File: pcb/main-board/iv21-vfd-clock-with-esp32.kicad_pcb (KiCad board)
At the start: 2 copper layers, 101.5 x 40 mm, 29 parts, among them J1 Conn_02x10_Odd_Even, J2 4328, P1 USB_C_Plug_USB2.0, SW1 SW_SPST, SW2 SW_SPST, U1 MAX6921AQI_, U2 MOUDLE-SEEEDUINO-XIAO-ESP32C3, U3 AP3012, U4 S-1167B24

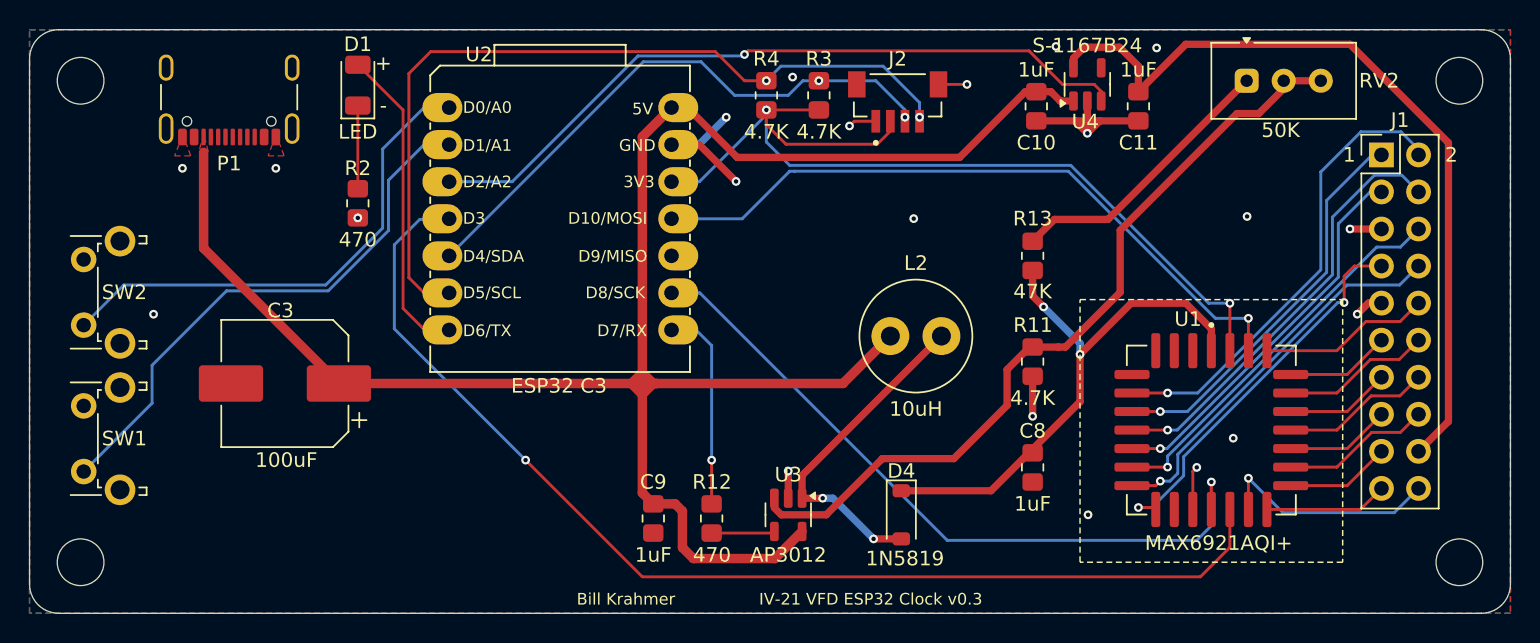
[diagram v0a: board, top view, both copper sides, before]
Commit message: Some trace updates.
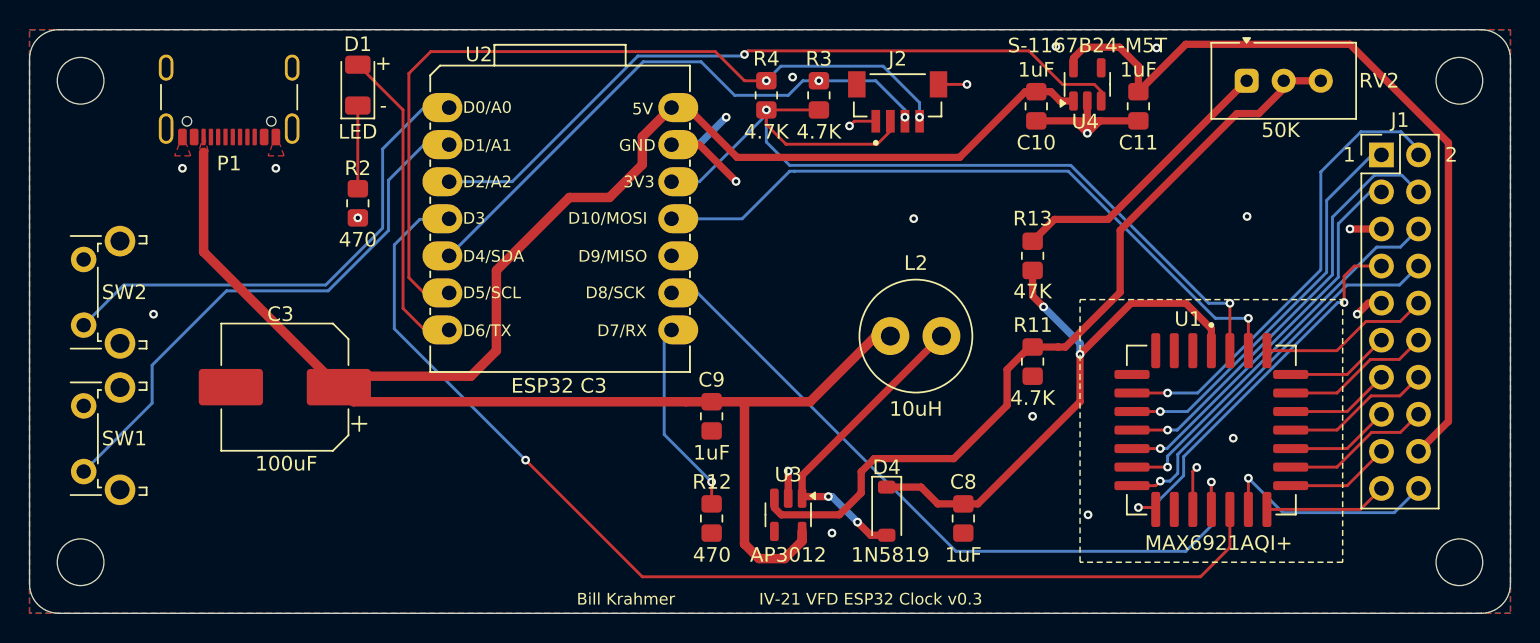
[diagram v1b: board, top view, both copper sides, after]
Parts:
- U4: value S-1167B24 -> S-1167B24-M5T
- moved C9 8.06 mm to (81.8, 44.5)
- moved C8 5.90 mm to (99.0, 51.5)
- moved D4 1.03 mm to (93.8, 51.0)
- moved C3 0.25 mm to (52.5, 42.5)
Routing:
- net /5V: track 137.1 -> 141.9 mm
- net Net-(U3-~{SHDN}): track 4.35 -> 0.16 mm
- net GND: track 37.2 -> 34.5 mm, vias 21 -> 22
- net /VPP: track 37.9 -> 39.6 mm
- net Net-(D4-A): track 23.0 -> 22.0 mm
- net Net-(U3-FB): track 54.9 -> 55.7 mm
- net Net-(U1-CLK): track 49.3 -> 49.9 mm
- net Net-(U2-PB09_A7_D7_RX): track 14.0 -> 13.5 mm

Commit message: change resistor value.
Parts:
- R13: value 47K -> 75K
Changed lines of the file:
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@@
 			)
 		)
-		(property "Value" "47K"
+		(property "Value" "75K"
 			(at -2.45 0 0)
 			(layer "F.SilkS")

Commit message: ...
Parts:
- moved C9 1.00 mm to (80.8, 44.5)
- moved R12 1.00 mm to (80.8, 51.5)
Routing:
- net Net-(U3-~{SHDN}): track 0.16 -> 5.51 mm, vias 0 -> 2
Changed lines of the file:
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@@
 	(footprint "Resistor_SMD:R_0805_2012Metric_Pad1.20x1.40mm_HandSolder"
 		(layer "F.Cu")
-		(at 81.75 51.5 -90)
+		(at 80.75 51.5 -90)
 		(descr "Resistor SMD 0805 (2012 Metric), square (rectangular) end terminal, IPC-7351 nominal with elongated pad for handsoldering. (Body size source: IPC-SM-782 page 72, https://www.pcb-3d.com/wordpress/wp-content/uploads/ipc-sm-782a_amendment_1_and_2.pdf), generated with kicad-footprint-generator")
 		(tags "resistor handsolder")
@@
 	(footprint "Resistor_SMD:R_0805_2012Metric_Pad1.20x1.40mm_HandSolder"
 		(layer "F.Cu")
-		(at 81.75 44.5 -90)
+		(at 80.75 44.5 -90)
 		(descr "Resistor SMD 0805 (2012 Metric), square (rectangular) end terminal, IPC-7351 nominal with elongated pad for handsoldering. (Body size source: IPC-SM-782 page 72, https://www.pcb-3d.com/wordpress/wp-content/uploads/ipc-sm-782a_amendment_1_and_2.pdf), generated with kicad-footprint-generator")
 		(tags "resistor handsolder")
@@
 	)
 	(segment
+		(start 80.75 43.5)
+		(end 57.2 43.5)
+		(width 0.65)
+		(layer "F.Cu")
+		(net 11)
+	)
+	(segment
 		(start 85 54.25)
 		(end 84 53.25)
@@
 	)
 	(segment
-		(start 57.2 43.5)
-		(end 56.2 42.5)
-		(width 0.65)
-		(layer "F.Cu")
-		(net 11)
-	)
-	(segment
 		(start 79 23.34)
 		(end 77 25.34)
@@
 	)
 	(segment
-		(start 81.75 43.5)
-		(end 80 43.5)
+		(start 57.2 43.5)
+		(end 56.2 42.5)
 		(width 0.65)
 		(layer "F.Cu")
@@
 	)
 	(segment
-		(start 80 43.5)
-		(end 57.2 43.5)
-		(width 0.65)
-		(layer "F.Cu")
-		(net 11)
-	)
-	(segment
 		(start 88.5 43.5)
 		(end 84 43.5)
@@
 	(segment
 		(start 84 43.5)
-		(end 81.75 43.5)
+		(end 80.75 43.5)
 		(width 0.65)
 		(layer "F.Cu")
@@
 		(net 39)
 	)
+	(via
+		(at 80.75 52.5)
+		(size 0.6)
+		(drill 0.3)
+		(layers "F.Cu" "B.Cu")
+		(net 39)
+	)
+	(via
+		(at 86.05 52.3875)
+		(size 0.6)
+		(drill 0.3)
+		(layers "F.Cu" "B.Cu")
+		(net 39)
+	)
 	(segment
-		(start 81.75 50.5)
-		(end 81.75 49)
+		(start 86.05 52.3875)
+		(end 80.8625 52.3875)
+		(width 0.2)
+		(layer "B.Cu")
+		(net 39)
+	)
+	(segment
+		(start 80.8625 52.3875)
+		(end 80.75 52.5)
+		(width 0.2)
+		(layer "B.Cu")
+		(net 39)
+	)
+	(segment
+		(start 80.75 49)
+		(end 80.75 50.5)
 		(width 0.2)
 		(layer "F.Cu")
@@
 	)
 	(via
-		(at 81.75 49)
+		(at 80.75 49)
 		(size 0.6)
 		(drill 0.3)
@@
 	)
 	(segment
-		(start 78.5 45.75)
+		(start 78.5 46.75)
 		(end 78.5 39.08)
 		(width 0.2)
@@
 	)
 	(segment
-		(start 78.5 39.08)
-		(end 79 38.58)
+		(start 80.75 49)
+		(end 78.5 46.75)
 		(width 0.2)
 		(layer "B.Cu")
@@
 	)
 	(segment
-		(start 81.75 49)
-		(end 78.5 45.75)
+		(start 78.5 39.08)
+		(end 79 38.58)
 		(width 0.2)
 		(layer "B.Cu")

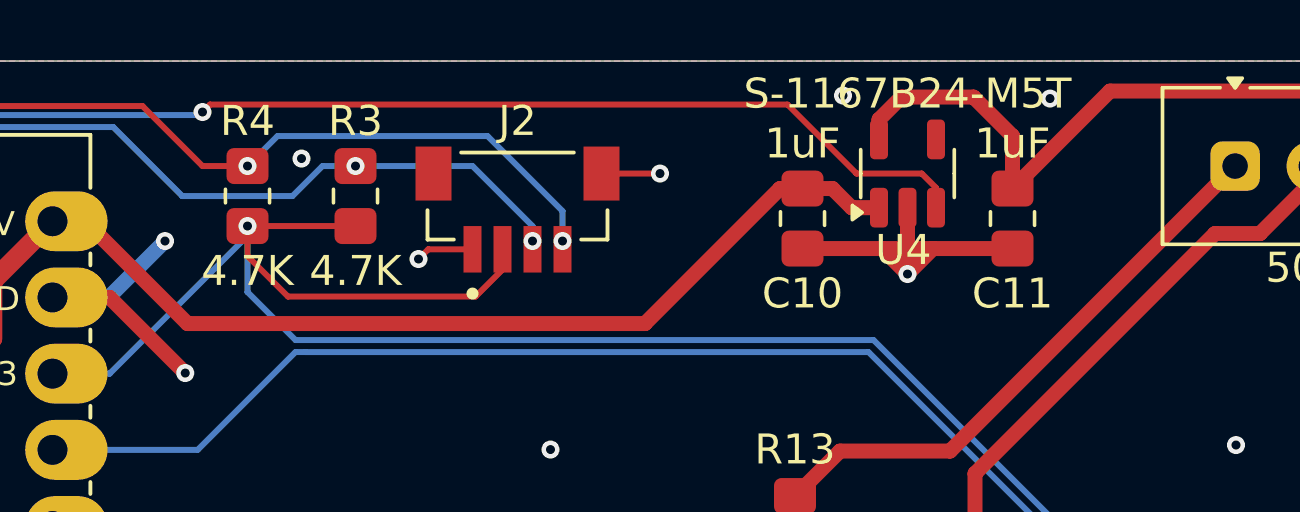
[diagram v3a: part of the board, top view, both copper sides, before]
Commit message: Add 470R resistor to S-1167B24 on/off pin
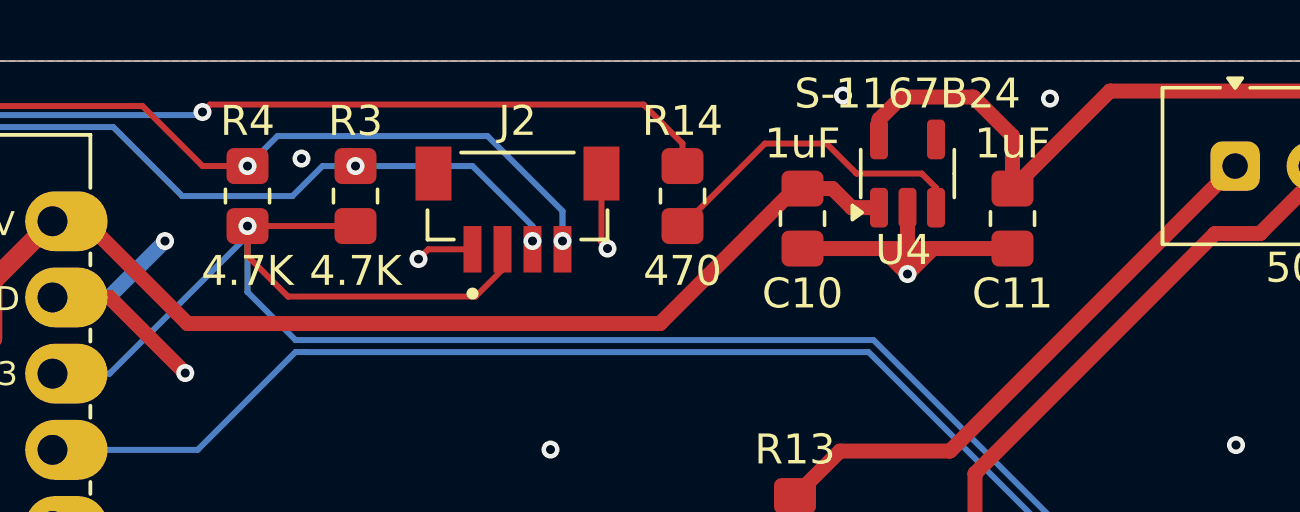
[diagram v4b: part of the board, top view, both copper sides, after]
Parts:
- added R14: 470, Resistor_SMD:R_0805_2012Metric_Pad1.20x1.40mm_HandSolder, F.Cu at (100.0, 22.5)
- U4: value S-1167B24-M5T -> S-1167B24
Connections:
- U4 pad 3: Net-(U2-PA10_A2_D2) -> Net-(U4-ON/~{OFF})
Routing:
- net Net-(U4-ON/~{OFF}): track 0.00 -> 10.9 mm
- net Net-(U2-PA10_A2_D2): track 50.2 -> 41.2 mm
- net GND: track 34.5 -> 35.1 mm
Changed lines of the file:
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@@
 	(net 52 "unconnected-(P1-SHIELD-PadS1)_2")
 	(net 53 "Net-(R13-Pad2)")
+	(net 54 "Net-(U4-ON{slash}~{OFF})")
 	(footprint "Diode_SMD:D_SOD-123"
 		(layer "F.Cu")
@@
 			)
 		)
-		(property "Value" "S-1167B24-M5T"
+		(property "Value" "S-1167B24"
 			(at 2.6625 0 0)
 			(layer "F.SilkS")
@@
 			(layers "F.Cu" "F.Mask" "F.Paste")
 			(roundrect_rratio 0.25)
-			(net 41 "Net-(U2-PA10_A2_D2)")
+			(net 54 "Net-(U4-ON{slash}~{OFF})")
 			(pinfunction "ON/~{OFF}")
 			(pintype "input")
@@
 		)
 	)
+	(footprint "Resistor_SMD:R_0805_2012Metric_Pad1.20x1.40mm_HandSolder"
+		(layer "F.Cu")
+		(at 100 22.5 90)
+		(descr "Resistor SMD 0805 (2012 Metric), square (rectangular) end terminal, IPC-7351 nominal with elongated pad for handsoldering. (Body size source: IPC-SM-782 page 72, https://www.pcb-3d.com/wordpress/wp-content/uploads/ipc-sm-782a_amendment_1_and_2.pdf), generated with kicad-footprint-generator")
+		(tags "resistor handsolder")
+		(property "Reference" "R14"
+			(at 2.5 0 0)
+			(layer "F.SilkS")
+			(effects
+				(font
+					(size 1 1)
+					(thickness 0.15)
+				)
+			)
+		)
+		(property "Value" "470"
+			(at -2.5 0 0)
+			(layer "F.SilkS")
+			(effects
+				(font
+					(size 1 1)
+					(thickness 0.15)
+				)
+			)
+		)
+		(property "Datasheet" ""
+			(at 0 0 90)
+			(layer "F.Fab")
+			(hide yes)
+			(effects
+				(font
+					(size 1.27 1.27)
+					(thickness 0.15)
+				)
+			)
+		)
+		(property "Description" "Resistor, US symbol"
+			(at 0 0 90)
+			(layer "F.Fab")
+			(hide yes)
+			(effects
+				(font
+					(size 1.27 1.27)
+					(thickness 0.15)
+				)
+			)
+		)
+		(property ki_fp_filters "R_*")
+		(sheetname "/")
+		(sheetfile "iv21-vfd-clock-with-esp32.kicad_sch")
+		(attr smd)
+		(fp_line
+			(start -0.227064 -0.735)
+			(end 0.227064 -0.735)
+			(stroke
+				(width 0.12)
+				(type solid)
+			)
+			(layer "F.SilkS")
+		)
+		(fp_line
+			(start -0.227064 0.735)
+			(end 0.227064 0.735)
+			(stroke
+				(width 0.12)
+				(type solid)
+			)
+			(layer "F.SilkS")
+		)
+		(fp_line
+			(start 1.85 -0.95)
+			(end 1.85 0.95)
+			(stroke
+				(width 0.05)
+				(type solid)
+			)
+			(layer "F.CrtYd")
+		)
+		(fp_line
+			(start -1.85 -0.95)
+			(end 1.85 -0.95)
+			(stroke
+				(width 0.05)
+				(type solid)
+			)
+			(layer "F.CrtYd")
+		)
+		(fp_line
+			(start 1.85 0.95)
+			(end -1.85 0.95)
+			(stroke
+				(width 0.05)
+				(type solid)
+			)
+			(layer "F.CrtYd")
+		)
+		(fp_line
+			(start -1.85 0.95)
+			(end -1.85 -0.95)
+			(stroke
+				(width 0.05)
+				(type solid)
+			)
+			(layer "F.CrtYd")
+		)
+		(fp_line
+			(start 1 -0.625)
+			(end 1 0.625)
+			(stroke
+				(width 0.1)
+				(type solid)
+			)
+			(layer "F.Fab")
+		)
+		(fp_line
+			(start -1 -0.625)
+			(end 1 -0.625)
+			(stroke
+				(width 0.1)
+				(type solid)
+			)
+			(layer "F.Fab")
+		)
+		(fp_line
+			(start 1 0.625)
+			(end -1 0.625)
+			(stroke
+				(width 0.1)
+				(type solid)
+			)
+			(layer "F.Fab")
+		)
+		(fp_line
+			(start -1 0.625)
+			(end -1 -0.625)
+			(stroke
+				(width 0.1)
+				(type solid)
+			)
+			(layer "F.Fab")
+		)
+		(fp_text user "${REFERENCE}"
+			(at 0 0 90)
+			(layer "F.Fab")
+			(effects
+				(font
+					(size 0.5 0.5)
+					(thickness 0.08)
+				)
+			)
+		)
+		(pad "1" smd roundrect
+			(at -1 0 90)
+			(size 1.2 1.4)
+			(layers "F.Cu" "F.Mask" "F.Paste")
+			(roundrect_rratio 0.208333)
+			(net 54 "Net-(U4-ON{slash}~{OFF})")
+			(pintype "passive")
+		)
+		(pad "2" smd roundrect
+			(at 1 0 90)
+			(size 1.2 1.4)
+			(layers "F.Cu" "F.Mask" "F.Paste")
+			(roundrect_rratio 0.208333)
+			(net 41 "Net-(U2-PA10_A2_D2)")
+			(pintype "passive")
+		)
+		(embedded_fonts no)
+		(model "${KICAD9_3DMODEL_DIR}/Resistor_SMD.3dshapes/R_0805_2012Metric.wrl"
+			(offset
+				(xyz 0 0 0)
+			)
+			(scale
+				(xyz 1 1 1)
+			)
+			(rotate
+				(xyz 0 0 0)
+			)
+		)
+	)
 	(footprint "Capacitor_SMD:CP_Elec_8x10.5"
 		(layer "F.Cu")
@@
 	)
 	(segment
-		(start 80.09 23.34)
-		(end 83.5 26.75)
-		(width 0.5)
+		(start 46.93 26.4)
+		(end 46.93 33.23)
+		(width 0.65)
 		(layer "F.Cu")
 		(net 11)
 	)
 	(segment
-		(start 46.93 26.4)
-		(end 46.93 33.23)
-		(width 0.65)
+		(start 79 23.34)
+		(end 80.09 23.34)
+		(width 0.5)
 		(layer "F.Cu")
 		(net 11)
@@
 	)
 	(segment
-		(start 46.93 24.98666)
-		(end 46.901109 24.957769)
-		(width 0.2)
+		(start 103.75 22.25)
+		(end 104 22.25)
+		(width 0.5)
 		(layer "F.Cu")
 		(net 11)
 	)
 	(segment
-		(start 103.25 22.25)
-		(end 104 22.25)
+		(start 83.5 26.75)
+		(end 99.25 26.75)
 		(width 0.5)
 		(layer "F.Cu")
@@
 	)
 	(segment
+		(start 46.93 24.98666)
+		(end 46.901109 24.957769)
+		(width 0.2)
+		(layer "F.Cu")
+		(net 11)
+	)
+	(segment
 		(start 65.25 41.75)
 		(end 56.95 41.75)
@@
 	)
 	(segment
-		(start 83.5 26.75)
-		(end 98.75 26.75)
-		(width 0.5)
+		(start 46.93 25.355)
+		(end 46.93 24.98666)
+		(width 0.2)
 		(layer "F.Cu")
 		(net 11)
 	)
 	(segment
-		(start 98.75 26.75)
-		(end 103.25 22.25)
+		(start 80.09 23.34)
+		(end 83.5 26.75)
 		(width 0.5)
 		(layer "F.Cu")
@@
 	)
 	(segment
-		(start 46.93 25.355)
-		(end 46.93 24.98666)
-		(width 0.2)
-		(layer "F.Cu")
-		(net 11)
-	)
-	(segment
 		(start 46.93 33.23)
 		(end 56.2 42.5)
@@
 	)
 	(segment
-		(start 79 23.34)
-		(end 80.09 23.34)
-		(width 0.5)
-		(layer "F.Cu")
-		(net 11)
-	)
-	(segment
 		(start 88.5 43.5)
 		(end 84 43.5)
@@
 	)
 	(segment
+		(start 99.25 26.75)
+		(end 103.75 22.25)
+		(width 0.5)
+		(layer "F.Cu")
+		(net 11)
+	)
+	(segment
 		(start 77 25.34)
 		(end 77 27.25)
@@
 	(segment
 		(start 97.3 21.75)
-		(end 99.25 21.75)
+		(end 97.3 24.05)
+		(width 0.2)
+		(layer "F.Cu")
+		(net 38)
+	)
+	(segment
+		(start 97.3 24.05)
+		(end 97.5 24.25)
 		(width 0.2)
 		(layer "F.Cu")
@@
 	)
 	(via
-		(at 99.25 21.75)
+		(at 97.5 24.25)
 		(size 0.6)
 		(drill 0.3)
@@
 	)
 	(segment
-		(start 84.25 19.45)
-		(end 84 19.7)
+		(start 98.7 19.45)
+		(end 100 20.75)
 		(width 0.2)
 		(layer "F.Cu")
@@
 	)
 	(segment
-		(start 105.8 21.75)
-		(end 103.5 19.45)
+		(start 84.25 19.45)
+		(end 98.7 19.45)
 		(width 0.2)
 		(layer "F.Cu")
@@
 	)
 	(segment
-		(start 103.5 19.45)
+		(start 84 19.7)
 		(end 84.25 19.45)
 		(width 0.2)
@@
 	)
 	(segment
-		(start 108.45 22.8875)
-		(end 108.45 22.225001)
-		(width 0.2)
-		(layer "F.Cu")
-		(net 41)
-	)
-	(segment
-		(start 108.45 22.225001)
-		(end 107.974999 21.75)
-		(width 0.2)
-		(layer "F.Cu")
-		(net 41)
-	)
-	(segment
-		(start 107.974999 21.75)
-		(end 105.8 21.75)
+		(start 100 20.75)
+		(end 100 21.5)
 		(width 0.2)
 		(layer "F.Cu")
@@
 		(net 53)
 	)
+	(segment
+		(start 104.8 20.75)
+		(end 102.75 20.75)
+		(width 0.2)
+		(layer "F.Cu")
+		(net 54)
+	)
+	(segment
+		(start 102.75 20.75)
+		(end 100 23.5)
+		(width 0.2)
+		(layer "F.Cu")
+		(net 54)
+	)
+	(segment
+		(start 108.45 22.8875)
+		(end 108.45 22.225001)
+		(width 0.2)
+		(layer "F.Cu")
+		(net 54)
+	)
+	(segment
+		(start 108.45 22.225001)
+		(end 107.974999 21.75)
+		(width 0.2)
+		(layer "F.Cu")
+		(net 54)
+	)
+	(segment
+		(start 107.974999 21.75)
+		(end 105.8 21.75)
+		(width 0.2)
+		(layer "F.Cu")
+		(net 54)
+	)
+	(segment
+		(start 105.8 21.75)
+		(end 104.8 20.75)
+		(width 0.2)
+		(layer "F.Cu")
+		(net 54)
+	)
 	(zone
